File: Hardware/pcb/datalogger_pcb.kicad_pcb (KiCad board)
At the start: 2 copper layers, 127.5 x 123.3 mm, 45 parts, among them J1 Micro_SD_Card_Det2, J2 Switch OUT, SW1 SW_Wuerth_450301014042, U1 DS3231MZ

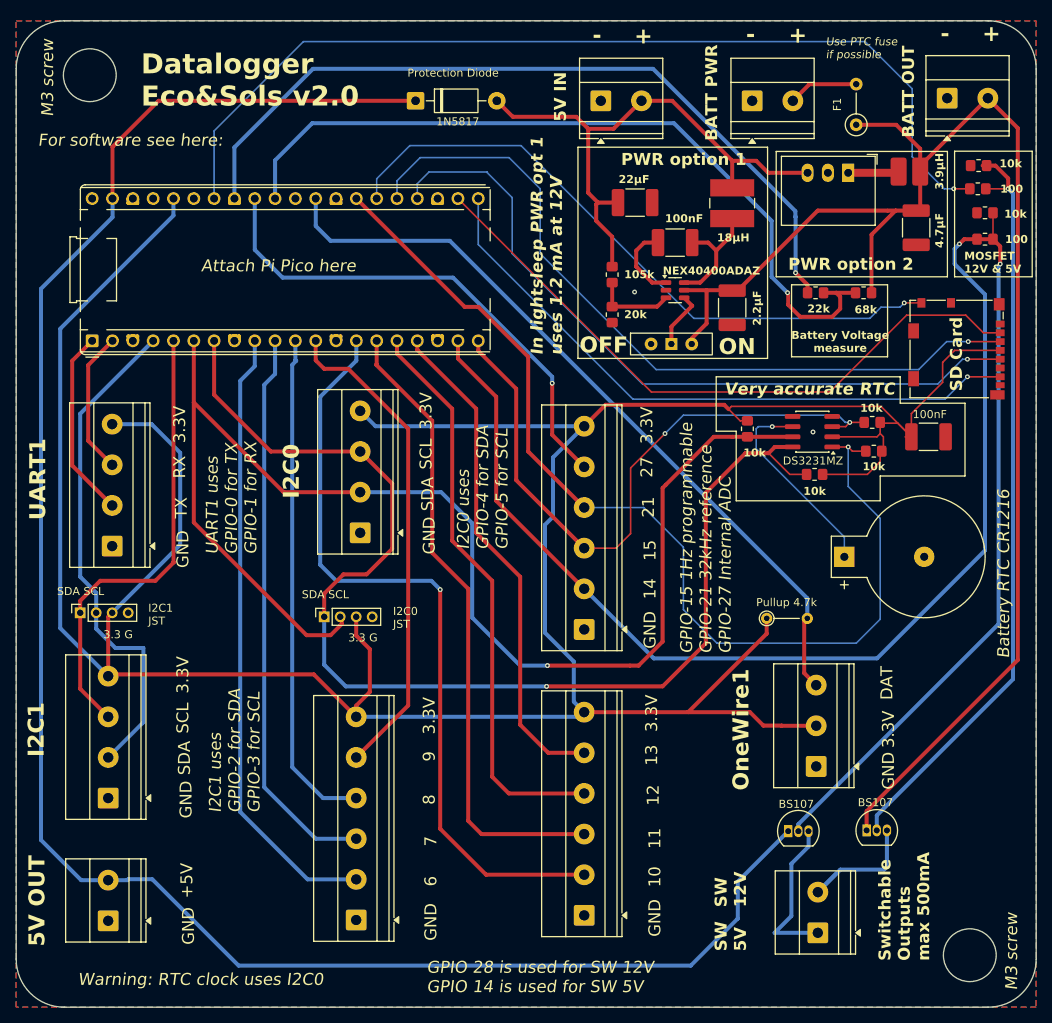
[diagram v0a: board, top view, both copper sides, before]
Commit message: Made cs616 work with new pcbs and disable pin
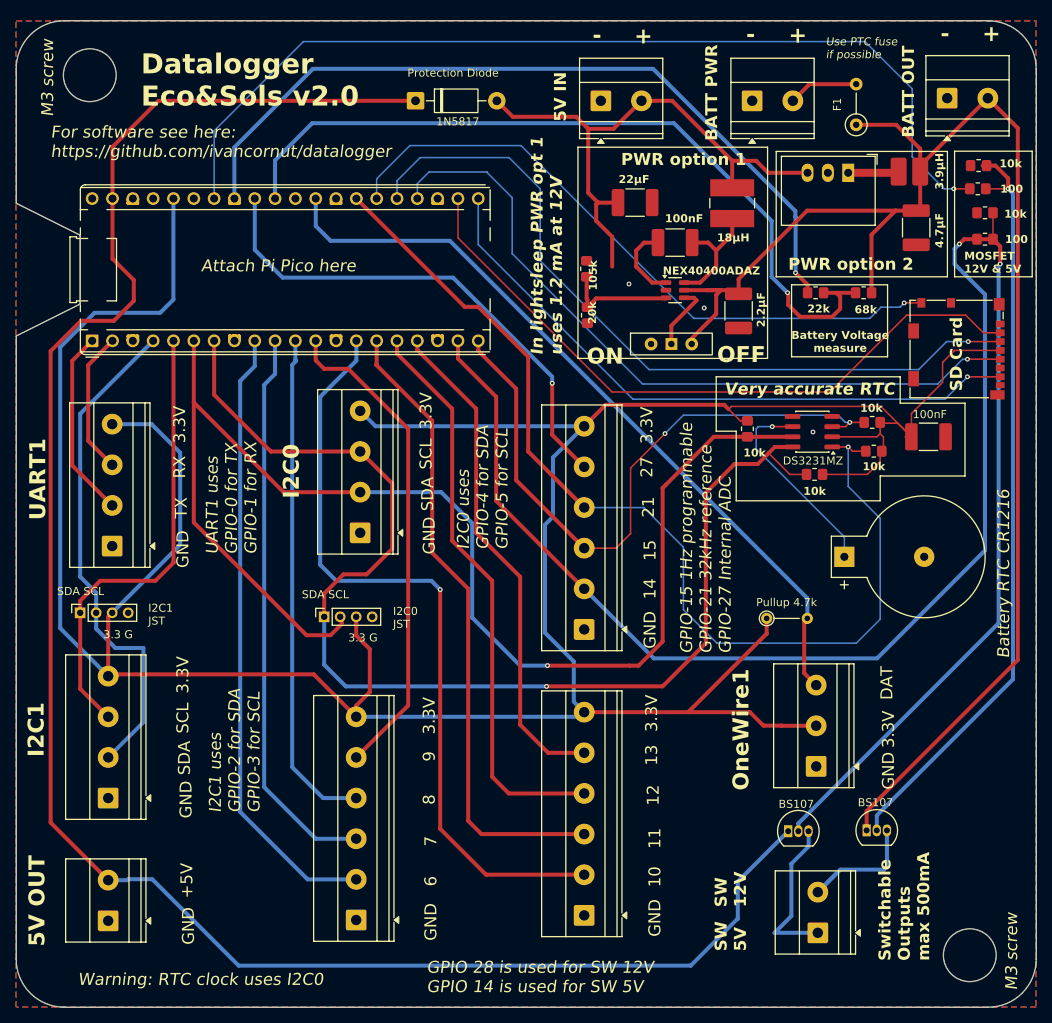
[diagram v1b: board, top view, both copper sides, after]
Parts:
- moved R3 3.28 mm to (121.3, 59.0)
- moved R4 3.10 mm to (121.4, 64.8)
- moved C2 0.89 mm to (140.3, 64.3)
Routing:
- net +3.3V: track 390.0 -> 394.8 mm
- net /FB: track 10.2 -> 14.2 mm
- net +12V: track 181.4 -> 184.8 mm
- net /CS: track 82.7 -> 85.6 mm
- net +5VP: track 240.3 -> 241.9 mm
- net Net-(Alimoption1-EN): track 6.57 -> 7.74 mm
- net /MOSI: track 96.0 -> 96.5 mm
- net GND: vias 2 -> 3
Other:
- outline, holes or cut-outs redrawn
- board text added: "For software see here: https://github.com/ivancornut/datalogger"
- board text removed: "For software see here:"

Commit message: Corrected screw diameter error
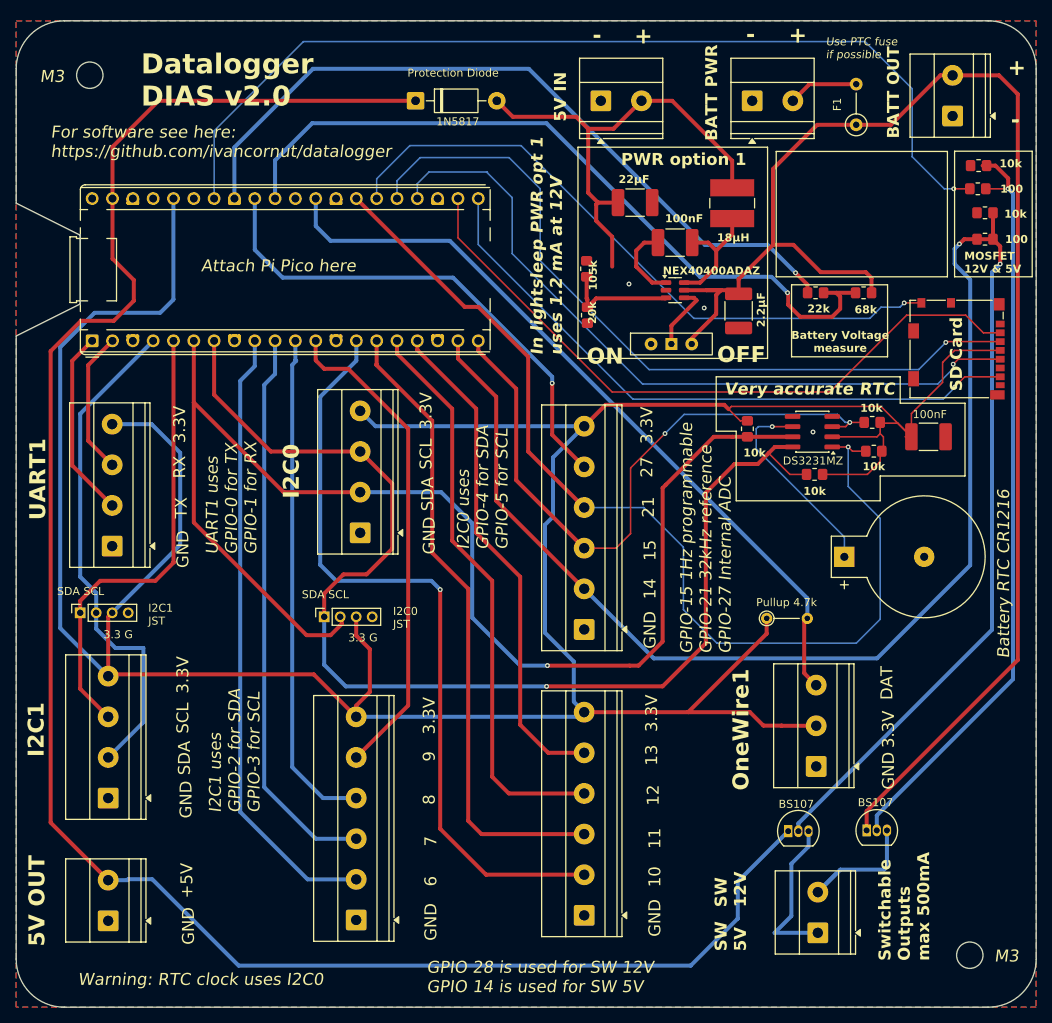
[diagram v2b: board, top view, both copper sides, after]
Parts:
- removed AlimOption2: R-78E5.0-0.5, Converter_DCDC:Converter_DCDC_RECOM_R-78E-0.5_THT
- removed C_alim2: 4.7 µF, Capacitor_SMD:C_1812_4532Metric_Pad1.57x3.40mm_HandSolder
- removed L_alim2: 3.9 µH, useful:RLS-397
- moved PWR12V1 2.33 mm to (167.1, 39.9), turned to 90 degrees
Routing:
- net +5V: track 70.0 -> 60.0 mm
- net Net-(AlimOption2-IN): track 6.36 -> 0.00 mm
- net /AGND: track 98.8 -> 94.3 mm
- net /READ12V: track 98.9 -> 94.8 mm
- net Net-(A1-GPIO14): track 139.1 -> 137.6 mm
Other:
- outline, holes or cut-outs redrawn
- board text added: "Datalogger DIAS v2.0"
- board text added: "M3"
- board text removed: "3.9µH"
- board text removed: "4.7µF"
- board text removed: "Datalogger Eco&Sols v2.0"
- board text removed: "M3 screw"
- board text removed: "PWR option 2"

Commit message: Added latching shutdown
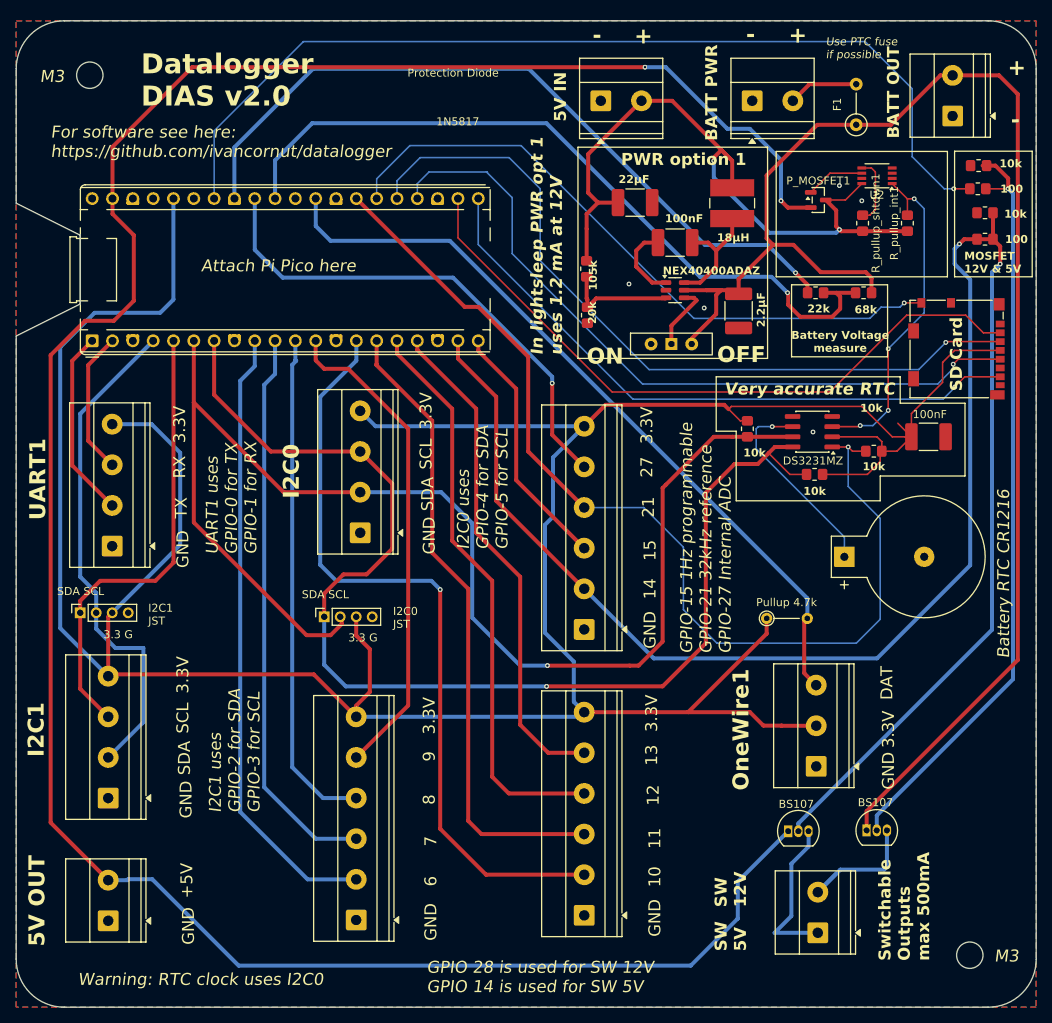
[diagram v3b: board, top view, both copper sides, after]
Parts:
- removed Diodeprotectionalim1: 1N5817, Diode_THT:D_DO-41_SOD81_P10.16mm_Horizontal
- removed R6: 10k, Resistor_SMD:R_0805_2012Metric_Pad1.20x1.40mm_HandSolder
- added P_MOSFET1: Si2319CDS, Package_TO_SOT_SMD:SOT-23, F.Cu at (150.3, 50.4)
- added R_pullup_int1: 100k, Resistor_SMD:R_0805_2012Metric_Pad1.20x1.40mm_HandSolder, F.Cu at (161.4, 53.3)
- added R_pullup_shtdwn1: 100k, Resistor_SMD:R_0805_2012Metric_Pad1.20x1.40mm_HandSolder, F.Cu at (155.8, 53.3)
- added U2: SN74LVC2G00DCTR, nand:SSOP-8_2.95x2.8mm_P0.65mm - SN74LVC2G00, F.Cu at (157.6, 47.4)
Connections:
- U1 pad 3: Net-(A1-GPIO15) -> /RTC_INT
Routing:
- net +5VP: track 241.9 -> 303.0 mm, vias 0 -> 2
- net Net-(A1-GPIO15): track 81.0 -> 31.4 mm, vias 2 -> 0
- net /RTC_INT: track 0.00 -> 42.4 mm, vias 0 -> 4
- net +5V: track 60.0 -> 92.5 mm, vias 0 -> 2
- net /SHTDWN_CTRL: track 0.00 -> 8.50 mm
- net Net-(P_MOSFET1-G): track 0.00 -> 7.37 mm
- net +12V: track 184.9 -> 185.6 mm
- net GND: vias 3 -> 5

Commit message: Added PAR sensor PCB
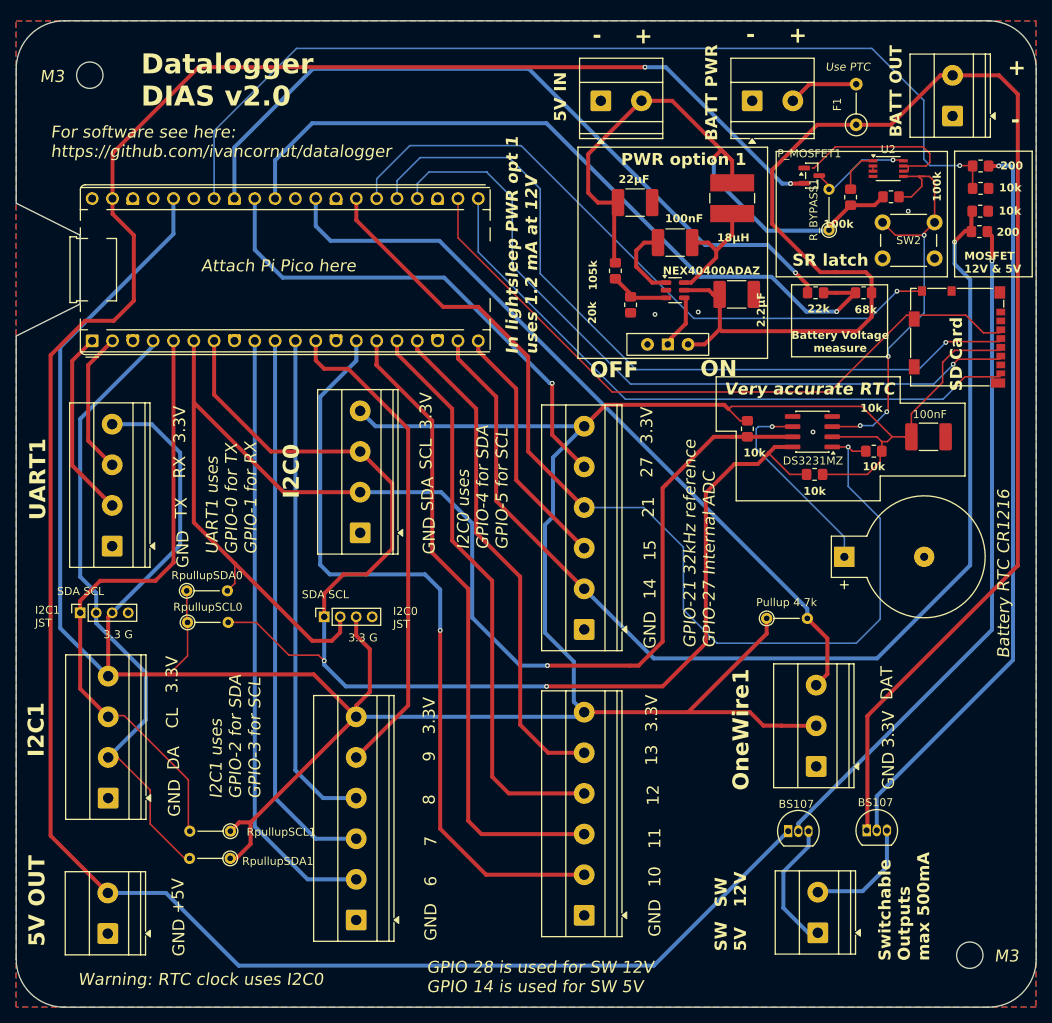
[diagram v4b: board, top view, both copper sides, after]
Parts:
- added R_BYPASS1: 0 Ohm, Resistor_THT:R_Axial_DIN0204_L3.6mm_D1.6mm_P5.08mm_Vertical, F.Cu at (151.6, 54.1)
- added RpullupSCL0: 10k, Resistor_THT:R_Axial_DIN0204_L3.6mm_D1.6mm_P5.08mm_Vertical, F.Cu at (71.4, 103.2)
- added RpullupSCL1: 10k, Resistor_THT:R_Axial_DIN0204_L3.6mm_D1.6mm_P5.08mm_Vertical, F.Cu at (76.8, 129.3)
- added RpullupSDA0: 10k, Resistor_THT:R_Axial_DIN0204_L3.6mm_D1.6mm_P5.08mm_Vertical, F.Cu at (71.3, 99.2)
- added RpullupSDA1: 10k, Resistor_THT:R_Axial_DIN0204_L3.6mm_D1.6mm_P5.08mm_Vertical, F.Cu at (76.8, 132.7)
- added SW2: SW_Push, Button_Switch_THT:SW_PUSH_6mm_H4.3mm, F.Cu at (164.8, 57.7)
- R7, R8: value R -> 100
- moved R_pullup_int1 7.81 mm to (154.3, 50.0)
- moved R4 5.55 mm to (126.8, 63.5)
- moved R_pullup_shtdwn1 4.85 mm to (159.3, 50.0), turned to 180 degrees
- moved R3 3.61 mm to (124.9, 59.2)
- moved P_MOSFET1 3.16 mm to (149.4, 47.4)
- moved R7 2.87 mm to (170.6, 46.1)
- moved R_pdown_MFET_1 2.86 mm to (170.6, 49.0), turned to 0 degrees
- moved C2 2.08 mm to (140.1, 62.2), turned to 0 degrees
- moved U2 1.66 mm to (159.0, 46.5), turned to 0 degrees
- moved 5VPOUT1 1.60 mm to (61.5, 142.1)
- moved J1 1.49 mm to (167.6, 67.5)
- moved R8 1.18 mm to (170.4, 54.4)
- moved R_pdown_MFET_2 0.63 mm to (170.5, 51.8), turned to 0 degrees
- moved L_alim1 0.62 mm to (139.5, 50.2)
- moved SW1 0.45 mm to (131.4, 68.5)
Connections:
- P_MOSFET1 pad 3: +5V -> Net-(P_MOSFET1-D)
- R_pdown_MFET_1 pad 1: Net-(MOSFET_12V1-G) -> Net-(A1-GPIO28_ADC2)
- R_pdown_MFET_2 pad 1: Net-(MOSFET_5V1-G) -> Net-(A1-GPIO14)
- R_pullup_int1 pad 2: /RTC_INT -> /SHTDWN_CTRL
- R_pullup_shtdwn1 pad 1: /SHTDWN_CTRL -> /RTC_INT
- U2 pad 1: /RTC_INT -> /SHTDWN_CTRL
- U2 pad 5: /SHTDWN_CTRL -> /RTC_INT
- U2 pad 8: +5V -> Net-(P_MOSFET1-D)
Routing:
- net +3.3V: track 395.0 -> 424.0 mm
- net /I2C1_SCL: track 57.4 -> 77.3 mm
- net +5V: track 92.5 -> 75.5 mm, vias 2 -> 1
- net /I2C1_SDA: track 63.4 -> 79.5 mm
- net /I2C0_SCL: track 150.4 -> 164.4 mm, vias 1 -> 2
- net Net-(P_MOSFET1-G): track 7.37 -> 20.8 mm
- net Net-(P_MOSFET1-D): track 0.00 -> 13.0 mm, vias 0 -> 1
- net /RTC_INT: track 42.4 -> 54.0 mm
- net +12V: track 185.6 -> 197.0 mm
- net +5VP: track 303.0 -> 295.7 mm
- net /FB: track 14.2 -> 7.62 mm
- net /I2C0_SDA: track 167.1 -> 171.8 mm
- net Net-(MOSFET_5V1-G): track 90.1 -> 85.5 mm
- net Net-(J2-Pin_1): track 19.9 -> 16.5 mm
- net Net-(J2-Pin_2): track 17.8 -> 14.5 mm
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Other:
- board text added: "100k"
- board text added: "200"
- board text added: "CL"
- board text added: "DA"
- board text added: "GPIO-21 32kHz reference GPIO-27 Internal ADC"
- board text added: "SR latch"
- board text added: "Use PTC"
- board text removed: "100"
- board text removed: "1N5817"
- board text removed: "GPIO-15 1Hz programmable GPIO-21 32kHz reference GPIO-27 Internal ADC"
- board text removed: "Protection Diode"
- board text removed: "Use PTC fuse if possible"
